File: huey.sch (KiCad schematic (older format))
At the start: 22 parts, among them CON1 BARREL_JACK, P1 TO_LEDS, P2 NPTC161KFXC-RC, P3 NPTC121KFXC-RC, P4 CONN_01X06, P5 CONN_01X02, P6 CONN_01X02, Q1 MF-DSC-SOT233-BSS138, U1 FEATHER_M0_WIFI

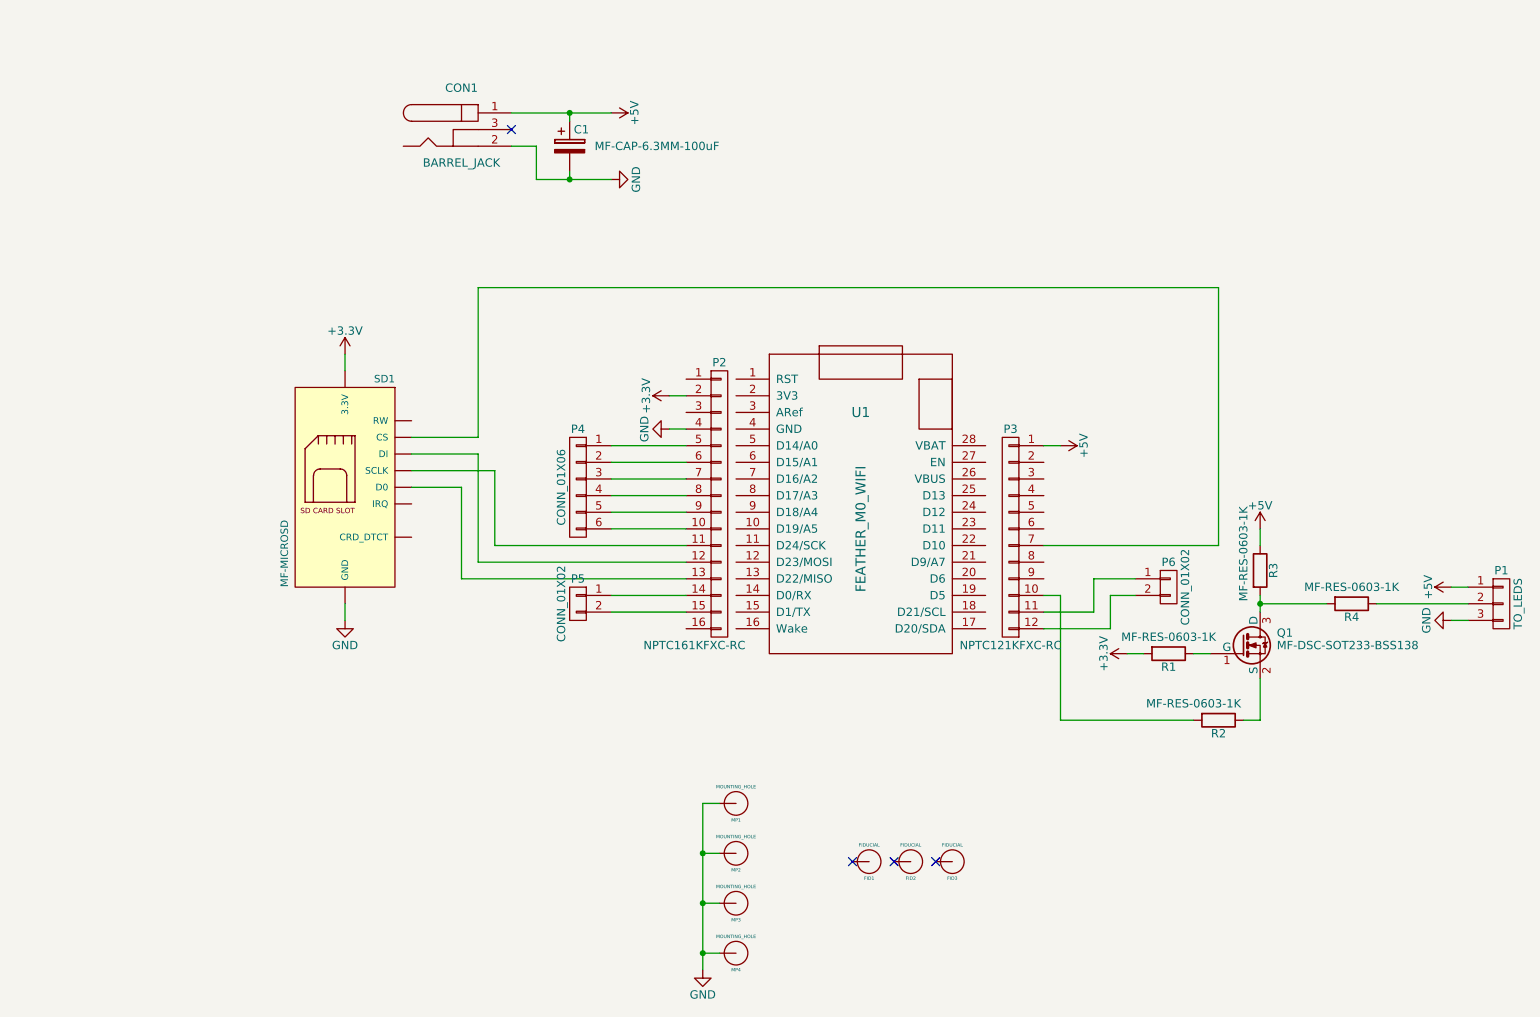
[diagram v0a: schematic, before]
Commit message: Some additions to the main board layout, and a new design of the top board.
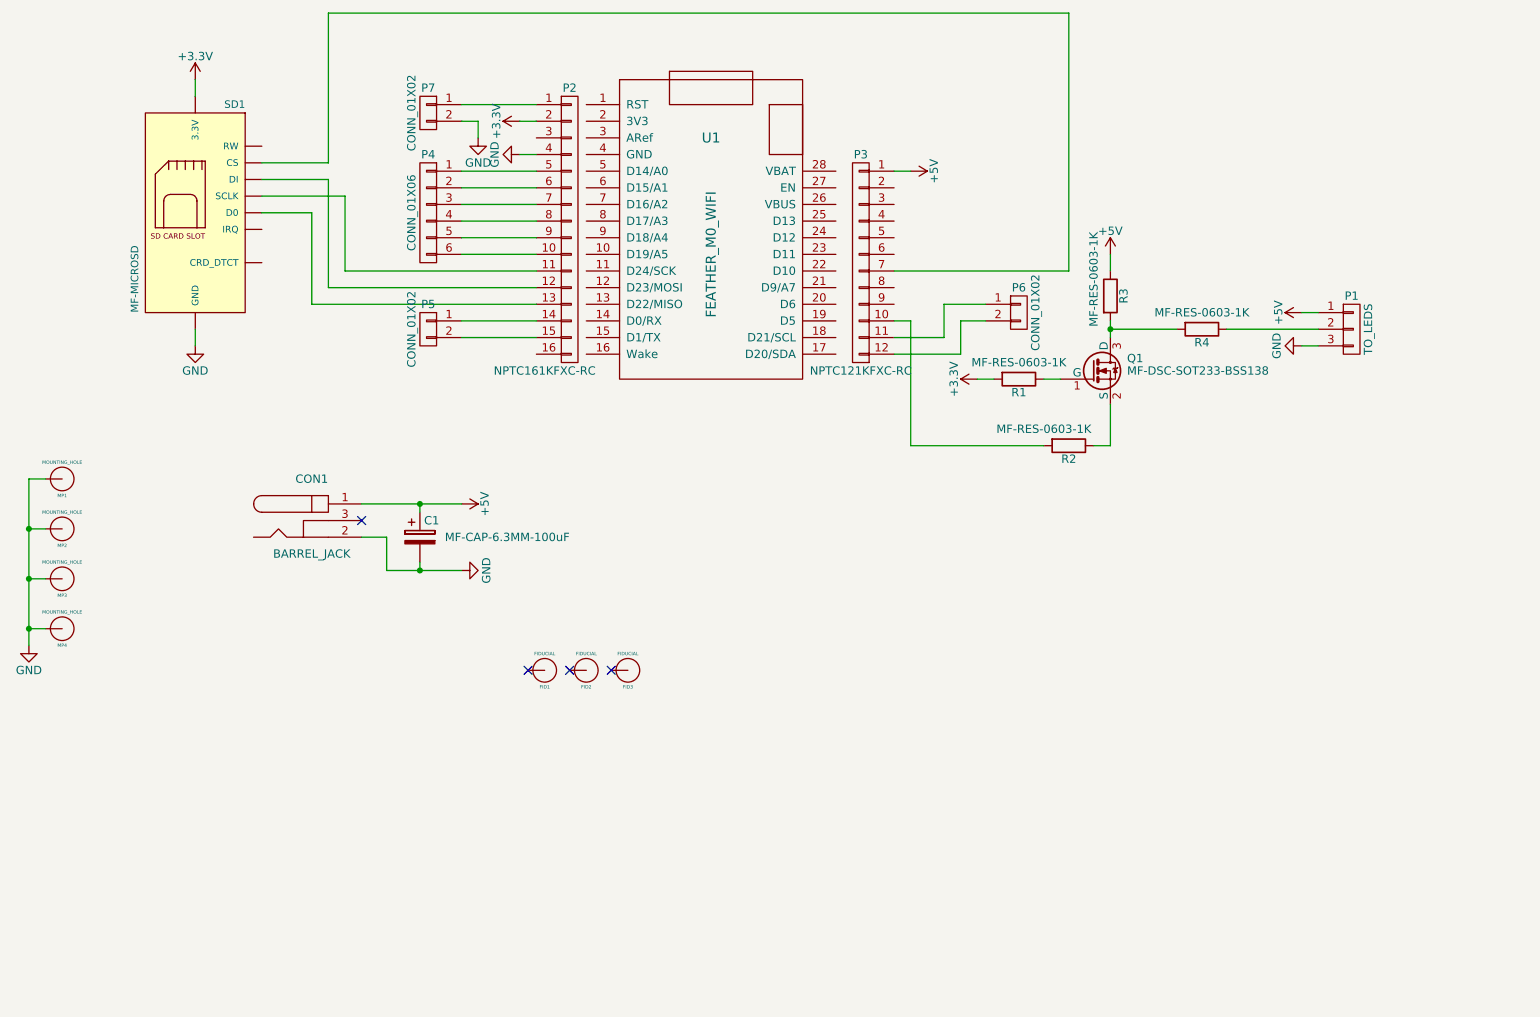
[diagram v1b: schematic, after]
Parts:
- added P7: CONN_01X02, Pin_Headers:Pin_Header_Straight_1x02, symbol CONN_01X02
- P1: footprint Pin_Headers:Pin_Header_Straight_1x03 -> Huey:LED_BOARD_CONNECTOR
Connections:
- net GND: now also P7.2 (P2)
- net at P2.1 (P1): now also P7.1 (P1)
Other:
- moved on the sheet: C1, CON1, FID1, FID2, FID3, MP1, MP2, MP3, MP4, P1, P2, P3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

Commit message: updating jack component
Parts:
- CON1: value BARREL_JACK -> PJ-036AH-SMT-TR
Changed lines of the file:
@@
 P 2700 4050
 F 0 "CON1" H 2700 4300 50  0000 C CNN
-F 1 "BARREL_JACK" H 2700 3850 50  0000 C CNN
+F 1 "PJ-036AH-SMT-TR" H 2700 3850 50  0000 C CNN
 F 2 "Huey:PJ-036AH-SMT-TR" H 2700 4050 50  0001 C CNN
 F 3 "" H 2700 4050 50  0000 C CNN

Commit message: Pushing final changes for rev 1.0
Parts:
- removed P2: NPTC161KFXC-RC, Huey:FEMALE_HEADER_16x1_SMD, symbol CONN_01X16
- added P2, P8: NPTC081KFXC-RC, Huey:FEMALE_HEADER_8x1_SMD, symbol CONN_01X08
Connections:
- net +3V3: now also P2.2 (P2)
- net GND: now also P2.4 (P4)
- net at SD1.3 (DI): now also P8.4 (P4)
- net at SD1.5 (SCLK): now also P8.3 (P3)
- net at SD1.7 (D0): now also P8.5 (P5)
- net at P7.1 (P1): now also P2.1 (P1)
- net at P4.6 (P6): now also P8.2 (P2)
- net at P5.1 (P1): now also P8.6 (P6)
- net at P5.2 (P2): now also P8.7 (P7)
- net at P4.1 (P1): now also P2.5 (P5)
- net at P4.2 (P2): now also P2.6 (P6)
- net at P4.3 (P3): now also P2.7 (P7)
- net at P4.4 (P4): now also P2.8 (P8)
- net at P4.5 (P5): now also P8.1 (P1)
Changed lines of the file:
@@
 	1100 4400 1000 4400
 Connection ~ 1000 4400
-$Comp
-L CONN_01X16 P2
-U 1 1 5ACB3909
-P 4250 2300
-F 0 "P2" H 4250 3150 50  0000 C CNN
-F 1 "NPTC161KFXC-RC" H 4100 1450 50  0000 C CNN
-F 2 "Huey:FEMALE_HEADER_16x1_SMD" H 4250 2300 50  0001 C CNN
-F 3 "" H 4250 2300 50  0000 C CNN
-F 4 "S5608-ND" H 4250 2300 60  0001 C CNN "Digikey"
-	1    4250 2300
-	1    0    0    -1
-$EndComp
 Wire Wire Line
 	3950 1650 4050 1650
@@
 Wire Wire Line
 	4050 1550 3600 1550
+$Comp
+L CONN_01X08 P2
+U 1 1 5ACD46B8
+P 4250 1900
+F 0 "P2" H 4250 2350 50  0000 C CNN
+F 1 "NPTC081KFXC-RC" V 4350 1900 50  0000 C CNN
+F 2 "Huey:FEMALE_HEADER_8x1_SMD" H 4250 1900 50  0001 C CNN
+F 3 "" H 4250 1900 50  0000 C CNN
+	1    4250 1900
+	1    0    0    -1
+$EndComp
+$Comp
+L CONN_01X08 P8
+U 1 1 5ACD4916
+P 4250 2700
+F 0 "P8" H 4250 3150 50  0000 C CNN
+F 1 "NPTC081KFXC-RC" V 4350 2700 50  0000 C CNN
+F 2 "Huey:FEMALE_HEADER_8x1_SMD" H 4250 2700 50  0001 C CNN
+F 3 "" H 4250 2700 50  0000 C CNN
+	1    4250 2700
+	1    0    0    -1
+$EndComp
 $EndSCHEMATC

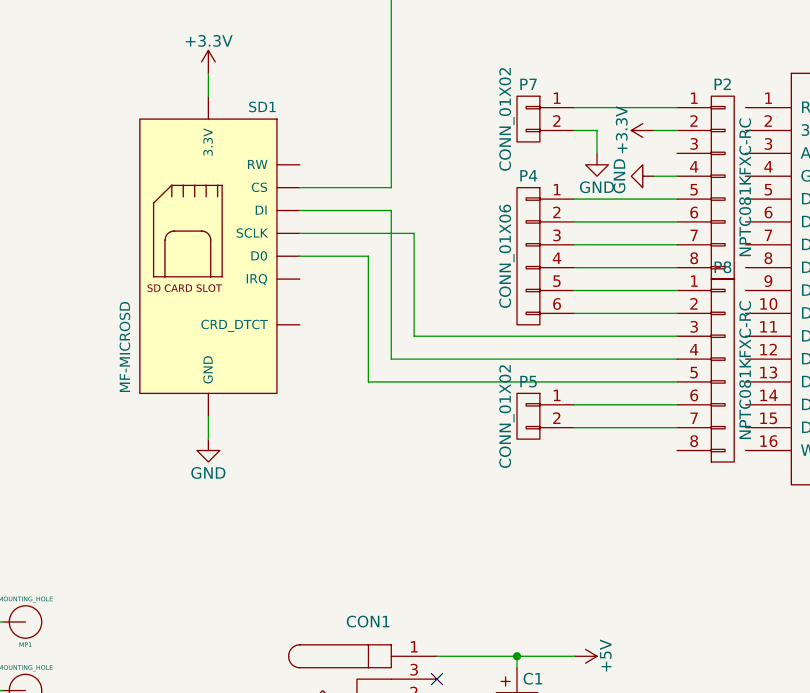
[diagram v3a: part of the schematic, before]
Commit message: Revision 1.1
Changelog:
-Re-exported copper pours to correct issues in rev 1.0
-Moved SD card to bottom for increased space
-Increased the clearance of copper pours for easier visual verification
-Added some vias to GND underneath the power jack to compensate for reduced GND plane area after increasing clearance
-Added test points for SD card data access
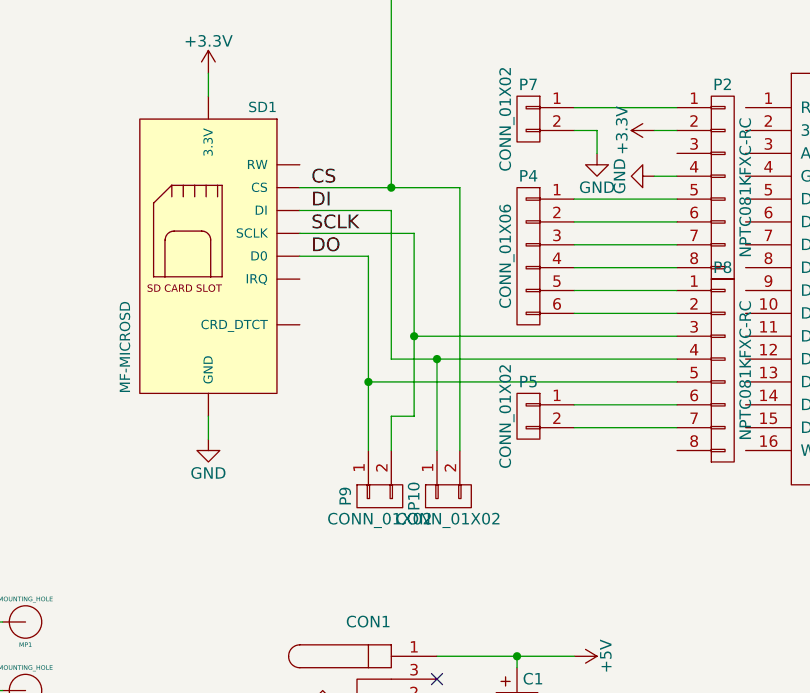
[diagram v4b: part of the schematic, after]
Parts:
- added P10, P9: CONN_01X02, Pin_Headers:Pin_Header_Straight_1x02, symbol CONN_01X02
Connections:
- net CS: now reaches P3.7 (P7), SD1.2 (CS)
- net CS: now also P10.2 (P2)
- net DI: now reaches P8.4 (P4), SD1.3 (DI)
- net DI: now also P10.1 (P1)
- net SCLK: now reaches P8.3 (P3), SD1.5 (SCLK)
- net SCLK: now also P9.2 (P2)
- net DO: now reaches P8.5 (P5), SD1.7 (D0)
- net DO: now also P9.1 (P1)
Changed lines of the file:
@@
 EESchema Schematic File Version 2
-LIBS:power
-LIBS:device
-LIBS:transistors
-LIBS:conn
-LIBS:linear
-LIBS:regul
-LIBS:74xx
-LIBS:cmos4000
-LIBS:adc-dac
-LIBS:memory
-LIBS:xilinx
-LIBS:microcontrollers
-LIBS:dsp
-LIBS:microchip
-LIBS:analog_switches
-LIBS:motorola
-LIBS:texas
-LIBS:intel
-LIBS:audio
-LIBS:interface
-LIBS:digital-audio
-LIBS:philips
-LIBS:display
-LIBS:cypress
-LIBS:siliconi
-LIBS:opto
-LIBS:atmel
-LIBS:contrib
-LIBS:valves
 LIBS:huey
 LIBS:MF_Connectors
@@
 Sheet 1 1
 Title "Huey Main Board"
-Date "2018-04-08"
-Rev "1.0"
+Date "2018-05-07"
+Rev "1.1"
 Comp "Kilo LLC"
 Comment1 ""
@@
 $EndComp
 Wire Wire Line
-	2700 2750 2700 2200
+	2700 2200 2700 3050
 Wire Wire Line
 	2700 2200 2400 2200
@@
 	2400 2000 2800 2000
 Wire Wire Line
-	2800 2000 2800 2650
-Wire Wire Line
-	2900 2550 2900 2100
+	2900 2100 2900 2900
 Wire Wire Line
 	2900 2100 2400 2100
@@
 	2800 1000 2800 1900
 Wire Wire Line
-	2800 1900 2400 1900
+	2400 1900 3100 1900
 $Comp
 L GND #PWR03
@@
 	1    0    0    -1
 $EndComp
+$Comp
+L CONN_01X02 P9
+U 1 1 5AF070D5
+P 2750 3250
+F 0 "P9" H 2750 3400 50  0000 C CNN
+F 1 "CONN_01X02" V 2850 3250 50  0000 C CNN
+F 2 "Pin_Headers:Pin_Header_Straight_1x02" H 2750 3250 50  0001 C CNN
+F 3 "" H 2750 3250 50  0000 C CNN
+	1    2750 3250
+	0    -1   1    0
+$EndComp
+$Comp
+L CONN_01X02 P10
+U 1 1 5AF0715A
+P 3050 3250
+F 0 "P10" H 3050 3400 50  0000 C CNN
+F 1 "CONN_01X02" V 3150 3250 50  0000 C CNN
+F 2 "Pin_Headers:Pin_Header_Straight_1x02" H 3050 3250 50  0001 C CNN
+F 3 "" H 3050 3250 50  0000 C CNN
+	1    3050 3250
+	0    -1   1    0
+$EndComp
+Connection ~ 2700 2750
+Wire Wire Line
+	3100 1900 3100 3050
+Connection ~ 2800 1900
+Wire Wire Line
+	3000 3050 3000 2650
+Connection ~ 3000 2650
+Wire Wire Line
+	2800 2000 2800 2650
+Wire Wire Line
+	2800 3050 2800 2900
+Wire Wire Line
+	2800 2900 2900 2900
+Connection ~ 2900 2550
+Text Label 2450 2200 0    60   ~ 0
+DO
+Text Label 2450 2100 0    60   ~ 0
+SCLK
+Text Label 2450 2000 0    60   ~ 0
+DI
+Text Label 2450 1900 0    60   ~ 0
+CS
 $EndSCHEMATC

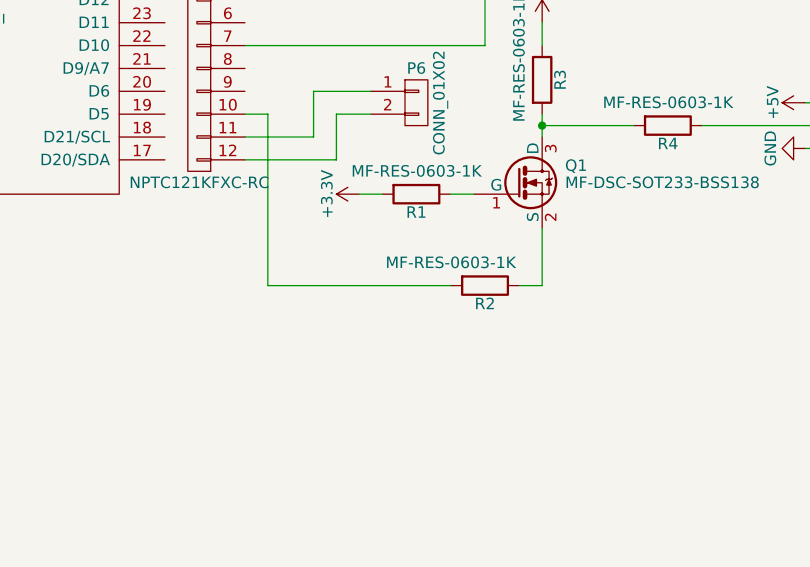
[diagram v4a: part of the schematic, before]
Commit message: Revision 1.1
Changelog:
	- Removed R2 resistor from the logic level converter
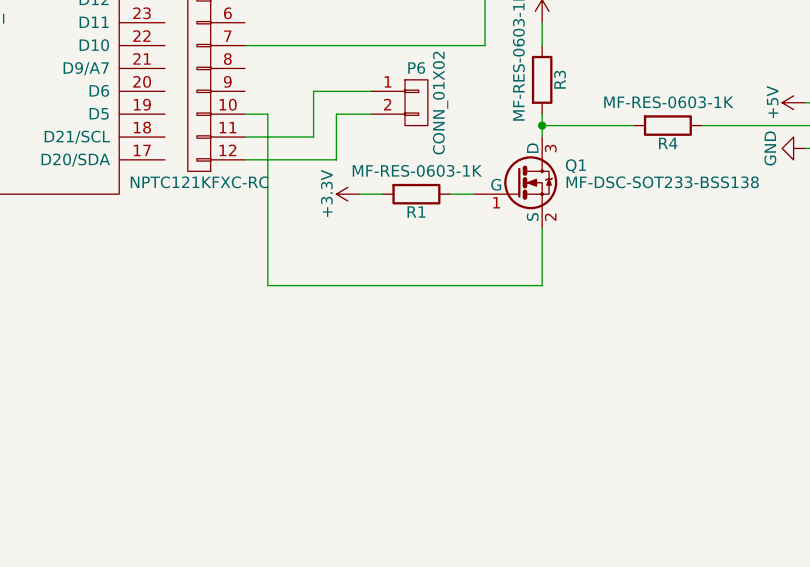
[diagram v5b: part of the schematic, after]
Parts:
- removed R2: MF-RES-0603-1K, Resistors_SMD:R_0603, symbol R
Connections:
- net at Q1.2 (S): now also P3.10 (P10)
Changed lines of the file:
@@
 EESchema Schematic File Version 2
+LIBS:power
+LIBS:device
+LIBS:transistors
+LIBS:conn
+LIBS:linear
+LIBS:regul
+LIBS:74xx
+LIBS:cmos4000
+LIBS:adc-dac
+LIBS:memory
+LIBS:xilinx
+LIBS:microcontrollers
+LIBS:dsp
+LIBS:microchip
+LIBS:analog_switches
+LIBS:motorola
+LIBS:texas
+LIBS:intel
+LIBS:audio
+LIBS:interface
+LIBS:digital-audio
+LIBS:philips
+LIBS:display
+LIBS:cypress
+LIBS:siliconi
+LIBS:opto
+LIBS:atmel
+LIBS:contrib
+LIBS:valves
 LIBS:huey
 LIBS:MF_Connectors
@@
 Wire Wire Line
 	2800 1000 2800 1900
-Wire Wire Line
-	2400 1900 3100 1900
 $Comp
 L GND #PWR03
@@
 Wire Wire Line
 	6700 3200 6800 3200
-$Comp
-L R R2
-U 1 1 5ACA81AB
-P 7250 3600
-F 0 "R2" V 7330 3600 50  0000 C CNN
-F 1 "MF-RES-0603-1K" V 7150 3450 50  0000 C CNN
-F 2 "Resistors_SMD:R_0603" V 7180 3600 50  0001 C CNN
-F 3 "" H 7250 3600 50  0000 C CNN
-	1    7250 3600
-	0    1    1    0
-$EndComp
-Wire Wire Line
-	7400 3600 7500 3600
-Wire Wire Line
-	6300 3600 7100 3600
+Wire Wire Line
+	6300 3600 7500 3600
 $Comp
 L R R4
@@
 Text Label 2450 1900 0    60   ~ 0
 CS
+Wire Wire Line
+	2400 1900 3100 1900
 $EndSCHEMATC

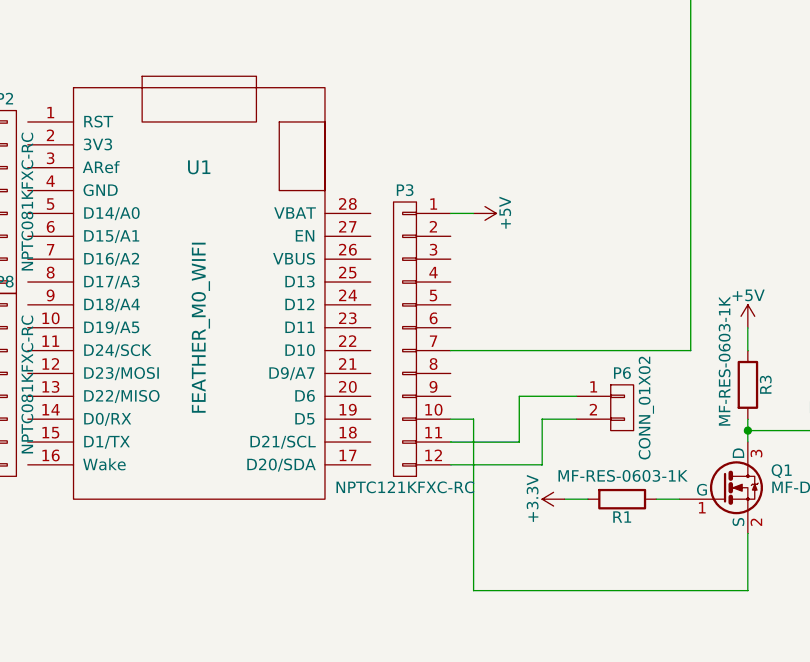
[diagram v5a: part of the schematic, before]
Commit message: Changing 12x1 SMD header to 8x1 and 4x1 headers, for (hopefully) better part availability
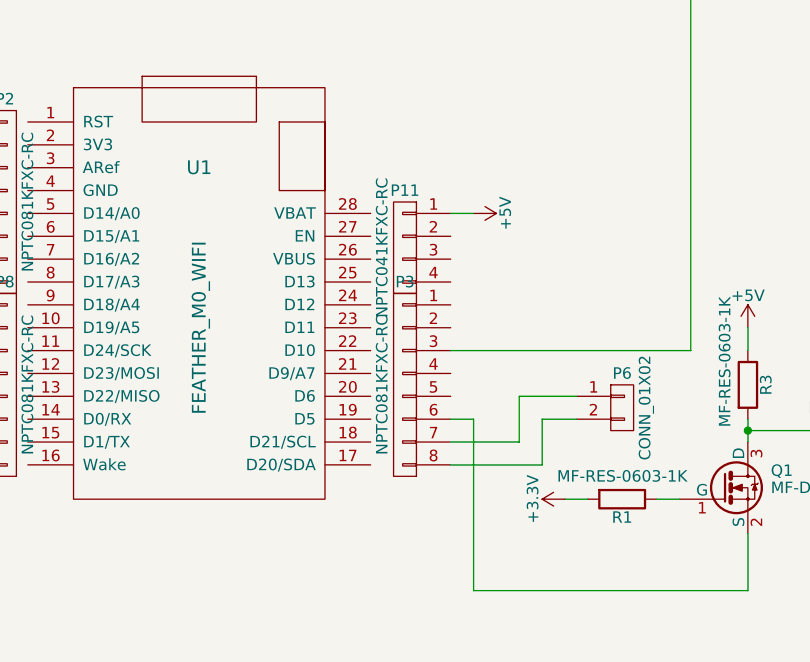
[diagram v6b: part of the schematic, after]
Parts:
- removed P3: NPTC121KFXC-RC, Huey:FEMALE_HEADER_12x1_SMD, symbol CONN_01X12
- added P11: NPTC041KFXC-RC, Huey:FEMALE_HEADER_04x1_SMD, symbol CONN_01X04
- added P3: NPTC081KFXC-RC, Huey:FEMALE_HEADER_8x1_SMD, symbol CONN_01X08
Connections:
- net +5V: now also P11.1 (P1)
- net CS: now also P3.3 (P3)
- net at Q1.2 (S): now also P3.6 (P6)
- net at P6.1 (P1): now also P3.7 (P7)
- net at P6.2 (P2): now also P3.8 (P8)
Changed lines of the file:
@@
 Title "Huey Main Board"
 Date "2018-05-07"
-Rev "1.1"
+Rev "1.2"
 Comp "Kilo LLC"
 Comment1 ""
@@
 Wire Wire Line
 	2700 2750 4050 2750
-$Comp
-L CONN_01X12 P3
-U 1 1 5ACB3E04
-P 6000 2500
-F 0 "P3" H 6000 3150 50  0000 C CNN
-F 1 "NPTC121KFXC-RC" H 6000 1850 50  0000 C CNN
-F 2 "Huey:FEMALE_HEADER_12x1_SMD" H 6000 2500 50  0001 C CNN
-F 3 "" H 6000 2500 50  0000 C CNN
-F 4 "S5604-ND" H 6000 2500 60  0001 C CNN "Digikey"
-	1    6000 2500
-	-1   0    0    -1
-$EndComp
 Wire Wire Line
 	6200 2850 6300 2850
@@
 Wire Wire Line
 	2400 1900 3100 1900
+$Comp
+L CONN_01X08 P3
+U 1 1 5B0DD788
+P 6000 2700
+F 0 "P3" H 6000 3150 50  0000 C CNN
+F 1 "NPTC081KFXC-RC" V 6100 2700 50  0000 C CNN
+F 2 "Huey:FEMALE_HEADER_8x1_SMD" H 6000 2700 50  0001 C CNN
+F 3 "" H 6000 2700 50  0000 C CNN
+	1    6000 2700
+	-1   0    0    -1
+$EndComp
+$Comp
+L CONN_01X04 P11
+U 1 1 5B0DD8D9
+P 6000 2100
+F 0 "P11" H 6000 2350 50  0000 C CNN
+F 1 "NPTC041KFXC-RC" V 6100 2100 50  0000 C CNN
+F 2 "Huey:FEMALE_HEADER_04x1_SMD" H 6000 2100 50  0001 C CNN
+F 3 "" H 6000 2100 50  0000 C CNN
+	1    6000 2100
+	-1   0    0    -1
+$EndComp
 $EndSCHEMATC
